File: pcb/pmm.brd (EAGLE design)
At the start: 30 x 30 mm, 25 parts, among them IC3 STM32F042F4, SW3 324_SW, SW4 324_SW, U2 USBC_16P, U4 XC6206_DEV

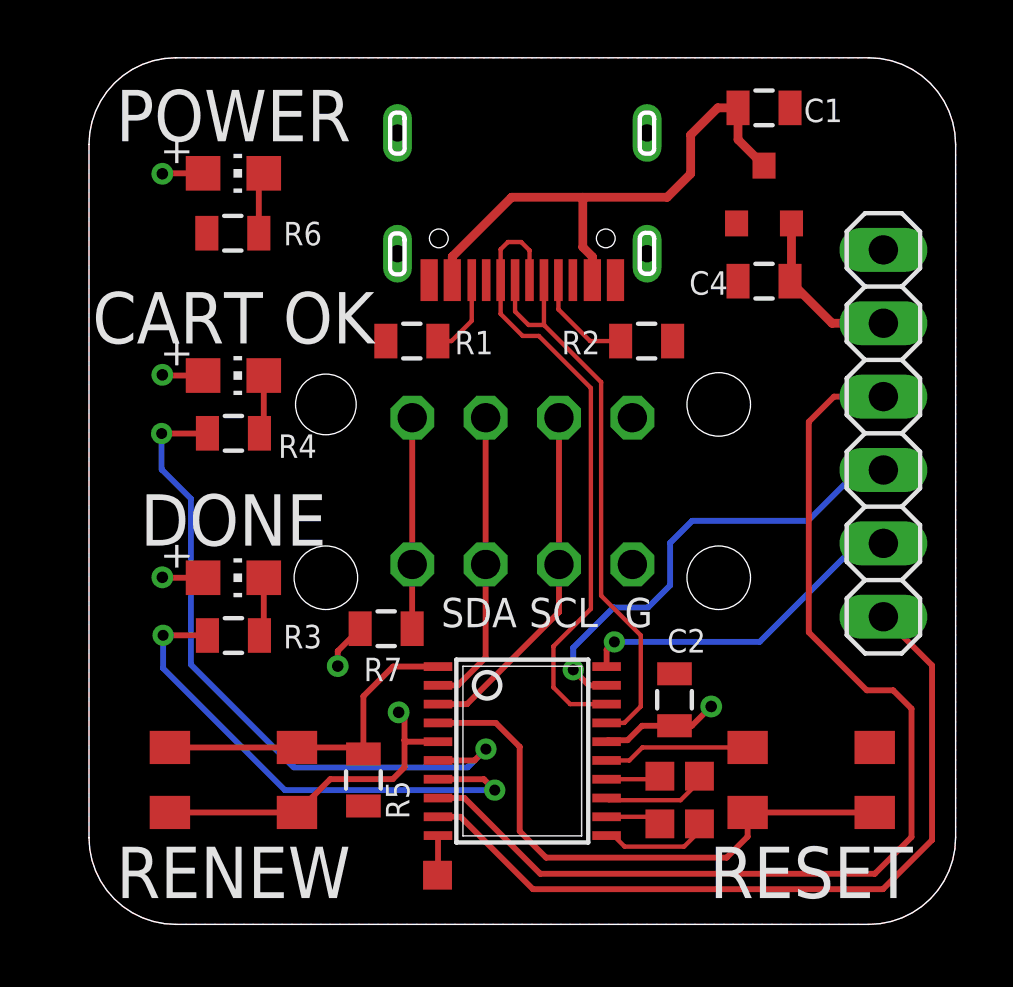
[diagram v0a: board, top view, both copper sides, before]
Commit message: updated component values
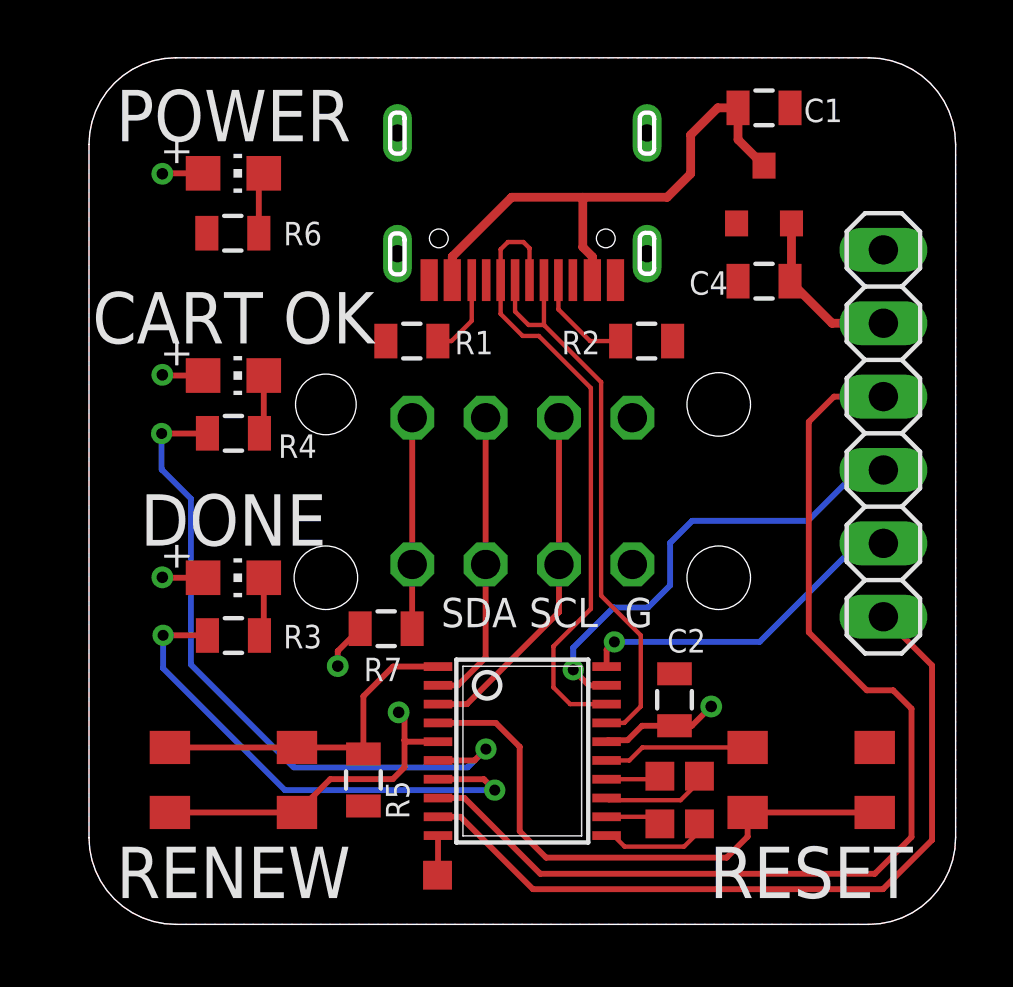
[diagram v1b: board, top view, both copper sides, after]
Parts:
- C1, C2: value 10uF -> 1uF
- C4: value 100nF -> 1uF
- R3, R4, R6, R7: value 2K -> 1K
- R5: value 10K -> 5.1K
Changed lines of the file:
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@@
 <grid distance="1" unitdist="mil" unit="mm" style="lines" multiple="1" display="no" altdistance="1" altunitdist="mil" altunit="mil"/>
 <layers>
-<layer number="1" name="Top" color="4" fill="1" visible="no" active="yes"/>
+<layer number="1" name="Top" color="4" fill="1" visible="yes" active="yes"/>
 <layer number="2" name="Route2" color="16" fill="1" visible="no" active="no"/>
 <layer number="3" name="Route3" color="17" fill="1" visible="no" active="no"/>
@@
 <layer number="19" name="Unrouted" color="6" fill="1" visible="yes" active="yes"/>
 <layer number="20" name="Dimension" color="24" fill="1" visible="yes" active="yes"/>
-<layer number="21" name="tPlace" color="7" fill="1" visible="no" active="yes"/>
+<layer number="21" name="tPlace" color="7" fill="1" visible="yes" active="yes"/>
 <layer number="22" name="bPlace" color="7" fill="1" visible="yes" active="yes"/>
-<layer number="23" name="tOrigins" color="15" fill="1" visible="no" active="yes"/>
+<layer number="23" name="tOrigins" color="15" fill="1" visible="yes" active="yes"/>
 <layer number="24" name="bOrigins" color="15" fill="1" visible="yes" active="yes"/>
-<layer number="25" name="tNames" color="7" fill="1" visible="no" active="yes"/>
+<layer number="25" name="tNames" color="7" fill="1" visible="yes" active="yes"/>
 <layer number="26" name="bNames" color="7" fill="1" visible="yes" active="yes"/>
-<layer number="27" name="tValues" color="7" fill="1" visible="no" active="yes"/>
+<layer number="27" name="tValues" color="7" fill="1" visible="yes" active="yes"/>
 <layer number="28" name="bValues" color="7" fill="1" visible="yes" active="yes"/>
 <layer number="29" name="tStop" color="7" fill="3" visible="no" active="yes"/>
@@
 <layer number="37" name="tTest" color="7" fill="1" visible="no" active="yes"/>
 <layer number="38" name="bTest" color="7" fill="1" visible="no" active="yes"/>
-<layer number="39" name="tKeepout" color="4" fill="11" visible="no" active="yes"/>
+<layer number="39" name="tKeepout" color="4" fill="11" visible="yes" active="yes"/>
 <layer number="40" name="bKeepout" color="1" fill="11" visible="yes" active="yes"/>
-<layer number="41" name="tRestrict" color="4" fill="10" visible="no" active="yes"/>
+<layer number="41" name="tRestrict" color="4" fill="10" visible="yes" active="yes"/>
 <layer number="42" name="bRestrict" color="1" fill="10" visible="yes" active="yes"/>
 <layer number="43" name="vRestrict" color="2" fill="10" visible="no" active="yes"/>
@@
 <layer number="49" name="Reference" color="7" fill="1" visible="no" active="yes"/>
 <layer number="50" name="dxf" color="7" fill="1" visible="no" active="no"/>
-<layer number="51" name="tDocu" color="7" fill="1" visible="no" active="yes"/>
+<layer number="51" name="tDocu" color="7" fill="1" visible="yes" active="yes"/>
 <layer number="52" name="bDocu" color="7" fill="1" visible="yes" active="yes"/>
 <layer number="53" name="tGND_GNDA" color="7" fill="1" visible="no" active="no"/>
@@
 <attribute name="NAME" x="17.6956" y="20.5478" size="0.8128" layer="25" rot="R180"/>
 </element>
-<element name="C1" library="clock" package="0805@1" value="10uF" x="23.3678" y="28.2666" smashed="yes" rot="R180">
+<element name="C1" library="clock" package="0805@1" value="1uF" x="23.3678" y="28.2666" smashed="yes" rot="R180">
 <attribute name="NAME" x="26.0856" y="28.5841" size="0.8128" layer="25" rot="R180"/>
 </element>
 <element name="IC3" library="tx" package="TSSOP20" value="STM32F042F4" x="15" y="6" smashed="yes" rot="R270"/>
-<element name="C4" library="clock" package="0805@1" value="100nF" x="23.3678" y="22.2666" smashed="yes">
+<element name="C4" library="clock" package="0805@1" value="1uF" x="23.3678" y="22.2666" smashed="yes">
 <attribute name="NAME" x="20.777" y="21.7967" size="0.8128" layer="25"/>
 </element>
@@
 <attribute name="VALUE" x="3.73" y="16.46" size="1.27" layer="27"/>
 </element>
-<element name="R4" library="SparkFun-Passives" package="0805" value="2K" x="5" y="17" smashed="yes">
+<element name="R4" library="SparkFun-Passives" package="0805" value="1K" x="5" y="17" smashed="yes">
 <attribute name="NAME" x="6.5494" y="16.1491" size="0.8128" layer="25"/>
 </element>
@@
 <attribute name="VALUE" x="3.73" y="23.46" size="1.27" layer="27"/>
 </element>
-<element name="R6" library="SparkFun-Passives" package="0805" value="2K" x="4.9784" y="23.9268" smashed="yes">
+<element name="R6" library="SparkFun-Passives" package="0805" value="1K" x="4.9784" y="23.9268" smashed="yes">
 <attribute name="NAME" x="6.731" y="23.5077" size="0.8128" layer="25"/>
 </element>
-<element name="R5" library="joyAnalog" package="0805" value="10K" x="9.4996" y="5" smashed="yes" rot="R90">
+<element name="R5" library="joyAnalog" package="0805" value="5.1K" x="9.4996" y="5" smashed="yes" rot="R90">
 <attribute name="NAME" x="10.2781" y="4.9784" size="0.8128" layer="25" rot="R270"/>
 </element>
@@
 </element>
 <element name="U4" library="3pos_slide_switch" package="SOT23R_INFINEON" value="XC6206_DEV" x="23.3678" y="25.2666" smashed="yes"/>
-<element name="C2" library="clock" package="0805@1" value="10uF" x="20.2692" y="7.7762" smashed="yes" rot="R270">
+<element name="C2" library="clock" package="0805@1" value="1uF" x="20.2692" y="7.7762" smashed="yes" rot="R270">
 <attribute name="NAME" x="20.0114" y="9.4107" size="0.8128" layer="25"/>
 </element>
@@
 <attribute name="VALUE" x="3.73" y="9.46" size="1.27" layer="27"/>
 </element>
-<element name="R3" library="SparkFun-Passives" package="0805" value="2K" x="5" y="10" smashed="yes">
+<element name="R3" library="SparkFun-Passives" package="0805" value="1K" x="5" y="10" smashed="yes">
 <attribute name="NAME" x="6.7272" y="9.5555" size="0.8128" layer="25"/>
 </element>
@@
 <attribute name="VALUE" x="30.675" y="9.38" size="1.27" layer="27" rot="R90"/>
 </element>
-<element name="R7" library="SparkFun-Passives" package="0805" value="2K" x="10.287" y="10.2362" smashed="yes" rot="R180">
+<element name="R7" library="SparkFun-Passives" package="0805" value="1K" x="10.287" y="10.2362" smashed="yes" rot="R180">
 <attribute name="NAME" x="10.8458" y="9.2329" size="0.8128" layer="25" rot="R180"/>
 </element>
@@
 <wire x1="14.25" y1="22.3025" x2="14.25" y2="23.3686" width="0.1524" layer="1"/>
 <wire x1="14.25" y1="23.3686" x2="14.5034" y2="23.622" width="0.1524" layer="1"/>
-<wire x1="14.5034" y1="23.622" x2="14.9606" y2="23.622" width="0.1524" layer="1"/>
-<wire x1="15.25" y1="23.3326" x2="15.25" y2="22.3025" width="0.1524" layer="1"/>
-<wire x1="14.9606" y1="23.622" x2="15.25" y2="23.3326" width="0.1524" layer="1"/>
+<wire x1="14.5034" y1="23.622" x2="15.0368" y2="23.622" width="0.1524" layer="1"/>
+<wire x1="15.25" y1="23.4088" x2="15.25" y2="22.3025" width="0.1524" layer="1"/>
+<wire x1="15.0368" y1="23.622" x2="15.25" y2="23.4088" width="0.1524" layer="1"/>
 </signal>
 <signal name="N$31">

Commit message: minor adjustments on PCB
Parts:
- moved R7 1.32 mm to (9.07, 9.73)
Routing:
- net N$10: track 7.31 -> 8.32 mm
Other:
- board text added: "GND"
- board text added: "VCC"

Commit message: updated pcb for next production run
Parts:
- removed SW3: 324_SW, 3pos_slide_switch_centered:342_SWICH_FOOT
- removed TP1, TP2, TP3, TP4, TP5: TPSQTP10SQ, testpad:TP10SQ
- added JP2: (no value), pinhead:2X03
- added U$1: PINHD1X2, adafruit_changed:1X02
- moved C2 1.69 mm to (20.7, 9.43)
- moved LED1 1.02 mm to (3.98, 19.0)
- moved LED2 1.02 mm to (3.98, 26.0)
- moved LED3 1.02 mm to (3.98, 12.0)
- moved R3 1.02 mm to (3.98, 10.0)
- moved R4 1.02 mm to (3.98, 17.0)
- moved R6 1.02 mm to (3.96, 23.9)
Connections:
- removed net BUTTON1: IC3.4, SW3.P$2, SW3.P$3
- new net N$16: IC3.10, U$1.1
- net GND: now also JP2.1; no longer SW3.P$1, SW3.P$4
- net N$11: now also IC3.11, JP2.4; no longer IC3.13, TP4.TP
- net N$12: now also JP2.6; no longer TP3.TP
- net N$13: now also IC3.13, JP2.3; no longer IC3.11, TP2.TP
- net N$14: now also JP2.5; no longer TP1.TP
- net N$15: now also IC3.4, JP2.2; no longer IC3.10, TP5.TP
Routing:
- net BUTTON1: track 19.9 -> 0.00 mm
- net N$15: track 1.38 -> 18.9 mm
- net GND: track 5.07 -> 0.00 mm
- net N$11: track 3.70 -> 6.58 mm
- net N$13: track 3.85 -> 6.72 mm
- net N$16: track 0.00 -> 2.17 mm
- net N$14: track 1.89 -> 3.84 mm
- net +3V3: track 27.5 -> 28.9 mm
- net N$12: track 1.94 -> 3.33 mm
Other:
- board text added: "3V"
- board text added: "A4"
- board text added: "A5"
- board text added: "A6"
- board text added: "A7"
- board text added: "B1"
- board text added: "F0"
- board text added: "F1"
- board text added: "RST"
- board text added: "bobRewind.com"
- board text added: "dekuNukem 2025"
- board text removed: "3V3"
- board text removed: "Bob Dishwasher Cassette Rewinder"
- board text removed: "RESET"
- board text removed: "dekuNukem 2021"
- board text removed: "git.io/bob_rewind"

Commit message: cleanup
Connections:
- net GND: now also U$1.2
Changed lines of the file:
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@@
 <contactref element="JP3" pad="6"/>
 <contactref element="JP2" pad="1"/>
+<contactref element="U$1" pad="2"/>
 </signal>
 <signal name="+3V3">
@@
 <contactref element="IC3" pad="10"/>
 <contactref element="U$1" pad="1"/>
-<wire x1="12.0822" y1="3.075" x2="12.0822" y2="2.1418" width="0.2032" layer="1"/>
-<wire x1="12.0822" y1="2.1418" x2="12.954" y2="1.27" width="0.2032" layer="1"/>
+<wire x1="12.0822" y1="3.075" x2="12.165" y2="3.075" width="0.2032" layer="1"/>
+<wire x1="12.954" y1="2.286" x2="12.165" y2="3.075" width="0.2032" layer="1"/>
+<wire x1="12.954" y1="2.286" x2="12.954" y2="1.27" width="0.2032" layer="1"/>
 </signal>
 </signals>
